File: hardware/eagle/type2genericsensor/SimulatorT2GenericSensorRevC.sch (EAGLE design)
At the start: 10 parts

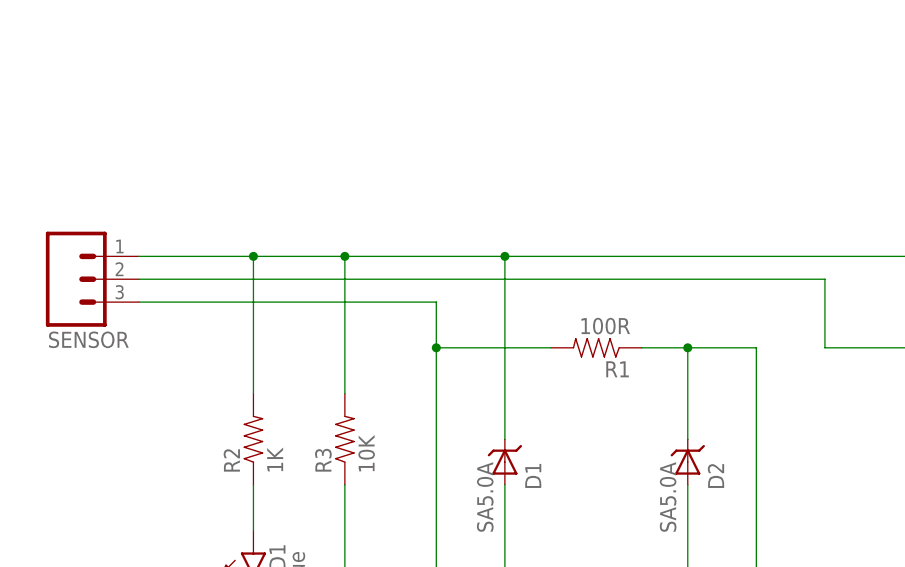
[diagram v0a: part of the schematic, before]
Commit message: Board Housekeeping
URL on silkscreens, caution messages, tidy up naming conventions.
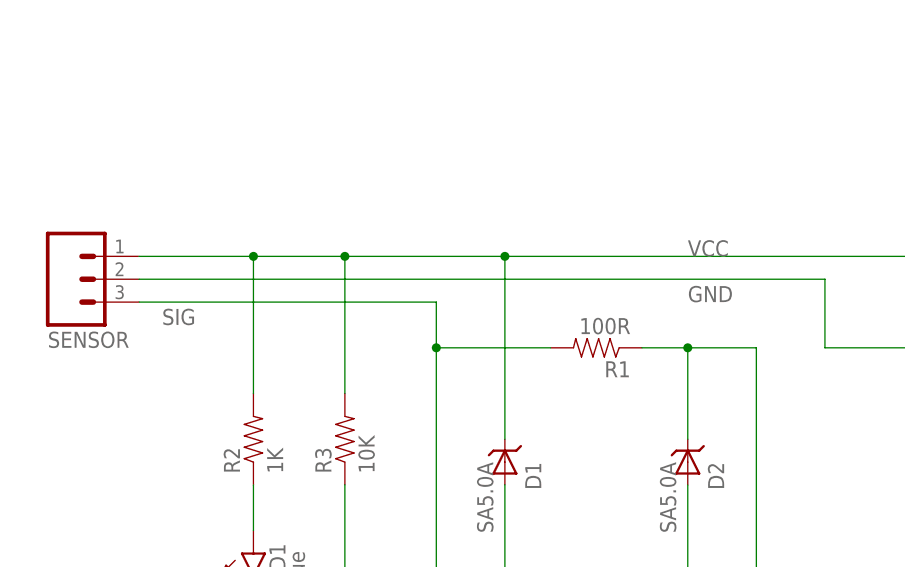
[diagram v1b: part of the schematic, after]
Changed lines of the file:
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@@
 <wire x1="149.86" y1="104.14" x2="165.1" y2="104.14" width="0.1524" layer="91"/>
 <junction x="165.1" y="104.14"/>
+<label x="134.62" y="109.22" size="1.778" layer="95"/>
 </segment>
 </net>
@@
 <wire x1="86.36" y1="114.3" x2="73.66" y2="114.3" width="0.1524" layer="91"/>
 <junction x="86.36" y="114.3"/>
+<label x="134.62" y="114.3" size="1.778" layer="95"/>
 </segment>
 </net>
@@
 <wire x1="106.68" y1="109.22" x2="73.66" y2="109.22" width="0.1524" layer="91"/>
 <junction x="106.68" y="104.14"/>
+<label x="76.2" y="106.68" size="1.778" layer="95"/>
 </segment>
 </net>
